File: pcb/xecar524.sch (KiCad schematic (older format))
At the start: 39 parts, among them J1 JTAG, J2 PROG, J3 Conn_02x02_Odd_Even, U1 MCP1703A-3302_SOT89, U2 Atari_XE_Cartridge_Connector, U3 XC95144XL-TQ100, U4 SST39VF040

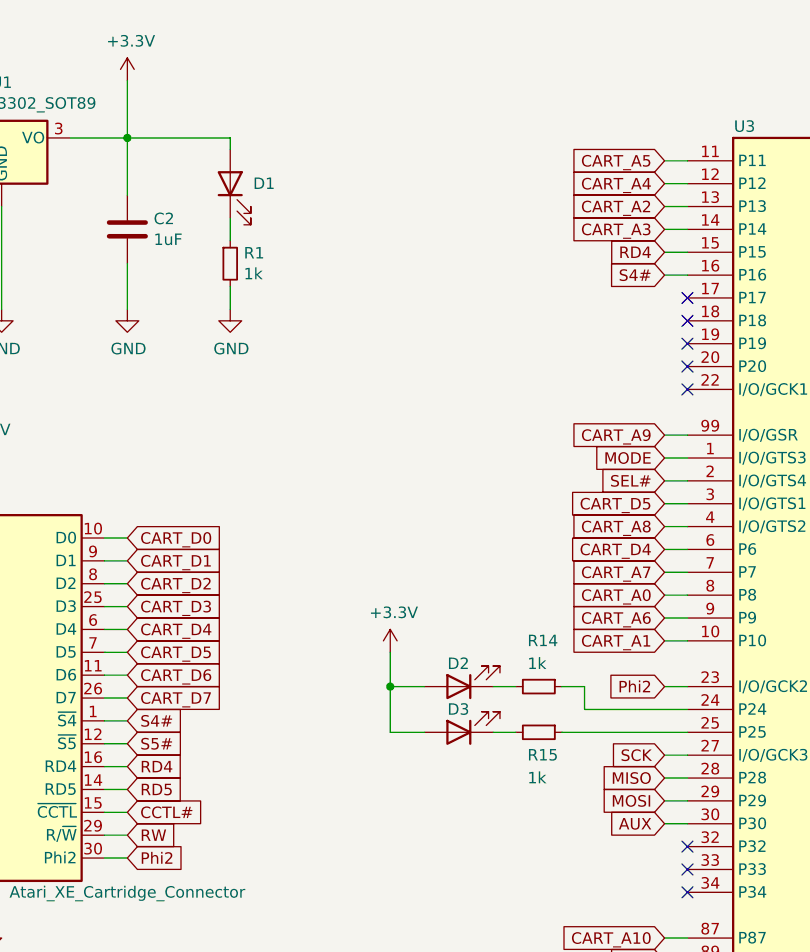
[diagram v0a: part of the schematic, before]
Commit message: PCB: Update LEDs and their current-setting resistors
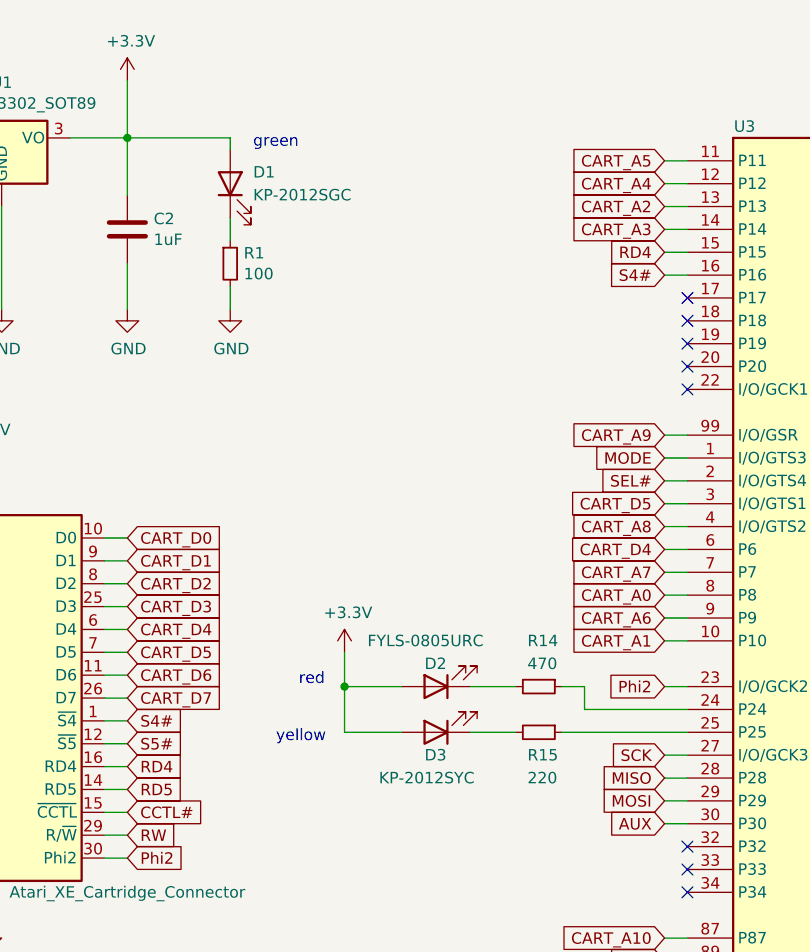
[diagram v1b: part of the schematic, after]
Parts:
- D1: value LED -> KP-2012SGC
- D2: value LED -> FYLS-0805URC
- D3: value LED -> KP-2012SYC
- R1: value 1k -> 100
- R14: value 1k -> 470
- R15: value 1k -> 220
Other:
- note added: "green"
- note added: "red"
- note added: "yellow"
- moved on the sheet: D2, D3
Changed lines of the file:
@@
 U 1 1 60C5727F
 P 2800 1350
-F 0 "D1" V 2800 1250 50  0000 R CNN
-F 1 "LED" V 2748 1232 50  0001 R CNN
+F 0 "D1" V 2850 1250 50  0000 R CNN
+F 1 "KP-2012SGC" V 2750 1250 50  0000 R CNN
 F 2 "Diode_SMD:D_0805_2012Metric_Pad1.15x1.40mm_HandSolder" H 2800 1350 50  0001 C CNN
 F 3 "~" H 2800 1350 50  0001 C CNN
@@
 P 2800 1700
 F 0 "R1" H 2859 1746 50  0000 L CNN
-F 1 "1k" H 2859 1655 50  0000 L CNN
+F 1 "100" H 2859 1655 50  0000 L CNN
 F 2 "Resistor_SMD:R_0805_2012Metric_Pad1.20x1.40mm_HandSolder" H 2800 1700 50  0001 C CNN
 F 3 "~" H 2800 1700 50  0001 C CNN
@@
 L Device:LED D3
 U 1 1 60DA2752
-P 3800 3750
-F 0 "D3" H 3850 3650 50  0000 R CNN
-F 1 "LED" H 4000 3700 50  0001 R CNN
-F 2 "Diode_SMD:D_0805_2012Metric_Pad1.15x1.40mm_HandSolder" H 3800 3750 50  0001 C CNN
-F 3 "~" H 3800 3750 50  0001 C CNN
-	1    3800 3750
+P 3700 3750
+F 0 "D3" H 3750 3850 50  0000 R CNN
+F 1 "KP-2012SYC" H 3950 3950 50  0000 R CNN
+F 2 "Diode_SMD:D_0805_2012Metric_Pad1.15x1.40mm_HandSolder" H 3700 3750 50  0001 C CNN
+F 3 "~" H 3700 3750 50  0001 C CNN
+	1    3700 3750
 	-1   0    0    1
 $EndComp
@@
 L Device:LED D2
 U 1 1 60DA08E3
-P 3800 3550
-F 0 "D2" H 3850 3450 50  0000 R CNN
-F 1 "LED" H 3748 3432 50  0001 R CNN
-F 2 "Diode_SMD:D_0805_2012Metric_Pad1.15x1.40mm_HandSolder" H 3800 3550 50  0001 C CNN
-F 3 "~" H 3800 3550 50  0001 C CNN
-	1    3800 3550
+P 3700 3550
+F 0 "D2" H 3750 3450 50  0000 R CNN
+F 1 "FYLS-0805URC" H 4000 3350 50  0000 R CNN
+F 2 "Diode_SMD:D_0805_2012Metric_Pad1.15x1.40mm_HandSolder" H 3700 3550 50  0001 C CNN
+F 3 "~" H 3700 3550 50  0001 C CNN
+	1    3700 3550
 	-1   0    0    1
 $EndComp
@@
 P 4150 3550
 F 0 "R14" V 3950 3500 50  0000 L CNN
-F 1 "1k" V 4050 3500 50  0000 L CNN
+F 1 "470" V 4050 3500 50  0000 L CNN
 F 2 "Resistor_SMD:R_0805_2012Metric_Pad1.20x1.40mm_HandSolder" H 4150 3550 50  0001 C CNN
 F 3 "~" H 4150 3550 50  0001 C CNN
@@
 P 4150 3750
 F 0 "R15" V 4250 3700 50  0000 L CNN
-F 1 "1k" V 4350 3700 50  0000 L CNN
+F 1 "220" V 4350 3700 50  0000 L CNN
 F 2 "Resistor_SMD:R_0805_2012Metric_Pad1.20x1.40mm_HandSolder" H 4150 3750 50  0001 C CNN
 F 3 "~" H 4150 3750 50  0001 C CNN
@@
 L power:+3.3V #PWR0117
 U 1 1 60DD9B32
-P 3500 3400
-F 0 "#PWR0117" H 3500 3250 50  0001 C CNN
-F 1 "+3.3V" H 3515 3573 50  0000 C CNN
-F 2 "" H 3500 3400 50  0001 C CNN
-F 3 "" H 3500 3400 50  0001 C CNN
-	1    3500 3400
-	1    0    0    -1
-$EndComp
-Wire Wire Line
-	3500 3400 3500 3550
-Wire Wire Line
-	3500 3550 3650 3550
+P 3300 3400
+F 0 "#PWR0117" H 3300 3250 50  0001 C CNN
+F 1 "+3.3V" H 3315 3573 50  0000 C CNN
+F 2 "" H 3300 3400 50  0001 C CNN
+F 3 "" H 3300 3400 50  0001 C CNN
+	1    3300 3400
+	1    0    0    -1
+$EndComp
+Wire Wire Line
+	3300 3400 3300 3550
 Wire Wire Line
 	4800 3750 4250 3750
 Wire Wire Line
-	3650 3750 3500 3750
-Wire Wire Line
-	3500 3750 3500 3550
-Connection ~ 3500 3550
+	3300 3750 3300 3550
+Connection ~ 3300 3550
 Wire Wire Line
 	4350 3550 4350 3650
@@
 	4350 3650 4800 3650
 Wire Wire Line
-	3950 3550 4050 3550
-Wire Wire Line
-	3950 3750 4050 3750
+	3850 3550 4050 3550
+Wire Wire Line
+	3850 3750 4050 3750
 Wire Wire Line
 	4250 3550 4350 3550
@@
 	-1   0    0    -1
 $EndComp
+Text Notes 2900 1200 0    50   ~ 0
+green
+Text Notes 3100 3550 0    50   ~ 0
+red
+Text Notes 3000 3800 0    50   ~ 0
+yellow
+Wire Wire Line
+	3300 3550 3550 3550
+Wire Wire Line
+	3300 3750 3550 3750
 $EndSCHEMATC

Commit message: PCB: Exchange cfg signals
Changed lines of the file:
@@
 	2400 5800 2400 5500
 Connection ~ 2400 5500
-Text GLabel 6900 1550 2    50   Input ~ 0
+Text GLabel 6900 1450 2    50   Input ~ 0
 CFG0
 Wire Wire Line
 	6900 1450 6800 1450
-Text GLabel 6900 1450 2    50   Input ~ 0
+Text GLabel 6900 1550 2    50   Input ~ 0
 CFG1
 Wire Wire Line
 	6900 1550 6800 1550
-$Comp
-L Connector_Generic:Conn_02x02_Odd_Even J3
-U 1 1 61481D01
-P 1600 5600
-F 0 "J3" H 1650 5725 50  0000 C CNN
-F 1 "Conn_02x02_Odd_Even" H 1650 5726 50  0001 C CNN
-F 2 "Connector_PinHeader_2.54mm:PinHeader_2x02_P2.54mm_Horizontal" H 1600 5600 50  0001 C CNN
-F 3 "~" H 1600 5600 50  0001 C CNN
-	1    1600 5600
-	-1   0    0    -1
-$EndComp
 Text Notes 2900 1200 0    50   ~ 0
 green
@@
 Wire Wire Line
 	3300 3750 3550 3750
+$Comp
+L Connector_Generic:Conn_02x02_Odd_Even J3
+U 1 1 61481D01
+P 1600 5700
+F 0 "J3" H 1650 5500 50  0000 C CNN
+F 1 "Conn_02x02_Odd_Even" H 1650 5826 50  0001 C CNN
+F 2 "Connector_PinHeader_2.54mm:PinHeader_2x02_P2.54mm_Horizontal" H 1600 5700 50  0001 C CNN
+F 3 "~" H 1600 5700 50  0001 C CNN
+	1    1600 5700
+	-1   0    0    1
+$EndComp
 $EndSCHEMATC

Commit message: PCB: Decrease yellow LED brightness
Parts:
- R15: value 220 -> 470
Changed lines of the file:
@@
 P 4150 3750
 F 0 "R15" V 4250 3700 50  0000 L CNN
-F 1 "220" V 4350 3700 50  0000 L CNN
+F 1 "470" V 4350 3700 50  0000 L CNN
 F 2 "Resistor_SMD:R_0805_2012Metric_Pad1.20x1.40mm_HandSolder" H 4150 3750 50  0001 C CNN
 F 3 "~" H 4150 3750 50  0001 C CNN

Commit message: PCB, PLD: Integrate R-Time 8 emulator
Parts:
- removed J2: PROG, Connector_PinHeader_2.54mm:PinHeader_1x08_P2.54mm_Horizontal_HighProfile, symbol Connector:Conn_01x08_Male
- removed R10, R11, R12, R13, R8, R9: 100, Resistor_SMD:R_0805_2012Metric_Pad1.20x1.40mm_HandSolder, symbol Device:R_Small
- removed R7: 10k, Resistor_SMD:R_0805_2012Metric_Pad1.20x1.40mm_HandSolder, symbol Device:R_Small
- U4: footprint Package_LCC:PLCC-32_THT-Socket -> Miscellaneous:PLCC-32_SMD-Socket
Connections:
- net labels added: PMCS1, PMD0, PMD1, PMD2, PMD3, PMRD, PMWR
- net labels removed: AUX, MISO, MODE, MOSI, SCK, SEL#
- wire segments 273 -> 254
- no-connect marks 12 -> 11
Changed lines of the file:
@@
 $Descr A4 11693 8268
 encoding utf-8
-Sheet 1 1
+Sheet 1 2
 Title ""
 Date ""
@@
 F 3 "http://atariki.krap.pl/index.php/Gniazdo_cartridge%27a" H 1700 3800 50  0001 C CNN
 	1    1750 3600
-	1    0    0    -1
-$EndComp
-$Comp
-L CPLD_Xilinx:XC95144XL-TQ100 U3
-U 1 1 61014D55
-P 5800 3650
-F 0 "U3" H 5050 6200 50  0000 C CNN
-F 1 "XC95144XL-TQ100" H 6600 1100 50  0000 C CNN
-F 2 "Package_QFP:TQFP-100_14x14mm_P0.5mm" H 5800 3650 50  0001 C CNN
-F 3 "https://www.xilinx.com/support/documentation/data_sheets/ds056.pdf" H 5800 3650 50  0001 C CNN
-	1    5800 3650
 	1    0    0    -1
 $EndComp
@@
 Wire Wire Line
 	6900 5450 6800 5450
-Text GLabel 6900 5550 2    50   Input ~ 0
+Text GLabel 6900 2450 2    50   Input ~ 0
 WE#
 Wire Wire Line
 	6900 5550 6800 5550
-Text GLabel 6900 2450 2    50   Input ~ 0
+Text GLabel 6900 2550 2    50   Input ~ 0
 ROM_A17
 Wire Wire Line
 	6900 2450 6800 2450
-Text GLabel 6900 2550 2    50   Input ~ 0
+Text GLabel 6900 2650 2    50   Input ~ 0
 ROM_A14
 Wire Wire Line
@@
 Wire Wire Line
 	6900 2650 6800 2650
-Text GLabel 6900 2650 2    50   Input ~ 0
+Text GLabel 6900 2750 2    50   Input ~ 0
 ROM_A13
+Text GLabel 6900 3650 2    50   Input ~ 0
+ROM_D6
 Text GLabel 6900 3550 2    50   Input ~ 0
-ROM_D6
+ROM_D7
+Text GLabel 6900 2150 2    50   Input ~ 0
+CE#
+Text GLabel 6900 1750 2    50   Input ~ 0
+OE#
+Wire Wire Line
+	6800 3550 6900 3550
+Wire Wire Line
+	6800 2050 6900 2050
+Wire Wire Line
+	6800 3650 6900 3650
+Wire Wire Line
+	6800 2150 6900 2150
 Text GLabel 6900 2050 2    50   Input ~ 0
-ROM_D7
-Text GLabel 6900 3650 2    50   Input ~ 0
-CE#
-Text GLabel 6900 2150 2    50   Input ~ 0
-OE#
-Wire Wire Line
-	6800 3550 6900 3550
-Wire Wire Line
-	6800 2050 6900 2050
-Wire Wire Line
-	6800 3650 6900 3650
-Wire Wire Line
-	6800 2150 6900 2150
-Text GLabel 6900 1750 2    50   Input ~ 0
 ROM_A10
 Wire Wire Line
@@
 Wire Wire Line
 	9450 5850 9200 5850
-$Comp
-L Connector:Conn_01x08_Male J2
-U 1 1 61185382
-P 1100 7050
-F 0 "J2" H 1208 7531 50  0000 C CNN
-F 1 "PROG" H 1208 7440 50  0000 C CNN
-F 2 "Connector_PinHeader_2.54mm:PinHeader_1x08_P2.54mm_Horizontal_HighProfile" H 1100 7050 50  0001 C CNN
-F 3 "~" H 1100 7050 50  0001 C CNN
-	1    1100 7050
-	1    0    0    -1
-$EndComp
-$Comp
-L Device:R_Small R10
-U 1 1 6118A684
-P 2000 7150
-F 0 "R10" V 1950 7000 50  0000 C CNN
-F 1 "100" V 1950 7300 50  0000 C CNN
-F 2 "Resistor_SMD:R_0805_2012Metric_Pad1.20x1.40mm_HandSolder" H 2000 7150 50  0001 C CNN
-F 3 "~" H 2000 7150 50  0001 C CNN
-	1    2000 7150
-	0    1    1    0
-$EndComp
-$Comp
-L Device:R_Small R11
-U 1 1 6118A8DE
-P 2000 7250
-F 0 "R11" V 1950 7100 50  0000 C CNN
-F 1 "100" V 1950 7400 50  0000 C CNN
-F 2 "Resistor_SMD:R_0805_2012Metric_Pad1.20x1.40mm_HandSolder" H 2000 7250 50  0001 C CNN
-F 3 "~" H 2000 7250 50  0001 C CNN
-	1    2000 7250
-	0    1    1    0
-$EndComp
-$Comp
-L Device:R_Small R12
-U 1 1 6118A8E8
-P 2000 7350
-F 0 "R12" V 1950 7200 50  0000 C CNN
-F 1 "100" V 1950 7500 50  0000 C CNN
-F 2 "Resistor_SMD:R_0805_2012Metric_Pad1.20x1.40mm_HandSolder" H 2000 7350 50  0001 C CNN
-F 3 "~" H 2000 7350 50  0001 C CNN
-	1    2000 7350
-	0    1    1    0
-$EndComp
-$Comp
-L Device:R_Small R13
-U 1 1 6118A8F2
-P 2000 7450
-F 0 "R13" V 1950 7300 50  0000 C CNN
-F 1 "100" V 1950 7600 50  0000 C CNN
-F 2 "Resistor_SMD:R_0805_2012Metric_Pad1.20x1.40mm_HandSolder" H 2000 7450 50  0001 C CNN
-F 3 "~" H 2000 7450 50  0001 C CNN
-	1    2000 7450
-	0    1    1    0
-$EndComp
-$Comp
-L Device:R_Small R9
-U 1 1 6118A8FC
-P 2000 7050
-F 0 "R9" V 1950 6900 50  0000 C CNN
-F 1 "100" V 1950 7200 50  0000 C CNN
-F 2 "Resistor_SMD:R_0805_2012Metric_Pad1.20x1.40mm_HandSolder" H 2000 7050 50  0001 C CNN
-F 3 "~" H 2000 7050 50  0001 C CNN
-	1    2000 7050
-	0    1    1    0
-$EndComp
-Wire Wire Line
-	1300 7250 1900 7250
-Wire Wire Line
-	1300 7350 1900 7350
-Wire Wire Line
-	1300 7450 1900 7450
-Wire Wire Line
-	2100 7450 2500 7450
-Wire Wire Line
-	2500 7350 2100 7350
-Wire Wire Line
-	2100 7250 2500 7250
-Wire Wire Line
-	2500 7150 2100 7150
-$Comp
-L power:GND #PWR01
-U 1 1 611A4CBD
-P 1400 6850
-F 0 "#PWR01" H 1400 6600 50  0001 C CNN
-F 1 "GND" V 1405 6722 50  0000 R CNN
-F 2 "" H 1400 6850 50  0001 C CNN
-F 3 "" H 1400 6850 50  0001 C CNN
-	1    1400 6850
-	0    -1   -1   0
-$EndComp
-Wire Wire Line
-	1400 6850 1300 6850
-$Comp
-L Device:R_Small R8
-U 1 1 611CD721
-P 2000 6950
-F 0 "R8" V 1950 6800 50  0000 C CNN
-F 1 "100" V 1950 7100 50  0000 C CNN
-F 2 "Resistor_SMD:R_0805_2012Metric_Pad1.20x1.40mm_HandSolder" H 2000 6950 50  0001 C CNN
-F 3 "~" H 2000 6950 50  0001 C CNN
-	1    2000 6950
-	0    1    1    0
-$EndComp
-$Comp
-L Device:R_Small R7
-U 1 1 611CDA81
-P 2000 6850
-F 0 "R7" V 1950 6700 50  0000 C CNN
-F 1 "10k" V 1950 7000 50  0000 C CNN
-F 2 "Resistor_SMD:R_0805_2012Metric_Pad1.20x1.40mm_HandSolder" H 2000 6850 50  0001 C CNN
-F 3 "~" H 2000 6850 50  0001 C CNN
-	1    2000 6850
-	0    1    1    0
-$EndComp
-Wire Wire Line
-	1300 7150 1900 7150
-Wire Wire Line
-	1300 7050 1900 7050
-Wire Wire Line
-	2500 6950 2300 6950
-Wire Wire Line
-	2100 7050 2500 7050
-Text GLabel 2500 6950 2    50   Input ~ 0
-MODE
-Text GLabel 2500 7050 2    50   Input ~ 0
-SEL#
-Text GLabel 2500 7250 2    50   Input ~ 0
-MOSI
-Text GLabel 2500 7350 2    50   Input ~ 0
-MISO
-$Comp
-L power:+3.3V #PWR02
-U 1 1 611B9BAC
-P 1750 6550
-F 0 "#PWR02" H 1750 6400 50  0001 C CNN
-F 1 "+3.3V" H 1765 6678 50  0000 L CNN
-F 2 "" H 1750 6550 50  0001 C CNN
-F 3 "" H 1750 6550 50  0001 C CNN
-	1    1750 6550
-	1    0    0    -1
-$EndComp
-Wire Wire Line
-	1300 6950 1900 6950
-Wire Wire Line
-	1300 6750 1750 6750
-Wire Wire Line
-	1750 6750 1750 6550
-Wire Wire Line
-	1900 6850 1750 6850
-Wire Wire Line
-	1750 6850 1750 6750
-Connection ~ 1750 6750
-Wire Wire Line
-	2100 6850 2300 6850
-Wire Wire Line
-	2300 6850 2300 6950
-Connection ~ 2300 6950
-Wire Wire Line
-	2300 6950 2100 6950
 Wire Wire Line
 	8150 5850 8750 5850
@@
 Wire Wire Line
 	6800 2750 6900 2750
-Text GLabel 6900 2750 2    50   Input ~ 0
+Text GLabel 6900 2850 2    50   Input ~ 0
 ROM_A8
 Wire Wire Line
 	6800 2850 6900 2850
-Text GLabel 6900 2850 2    50   Input ~ 0
+Text GLabel 6900 2950 2    50   Input ~ 0
 ROM_A9
 Wire Wire Line
 	6900 2950 6800 2950
-Text GLabel 6900 2950 2    50   Input ~ 0
+Text GLabel 6900 1650 2    50   Input ~ 0
 ROM_A11
 Wire Wire Line
@@
 Wire Wire Line
 	6900 3750 6800 3750
+Text GLabel 6900 3750 2    50   Input ~ 0
+ROM_D5
 Text GLabel 6900 3850 2    50   Input ~ 0
-ROM_D5
-Text GLabel 6900 3750 2    50   Input ~ 0
 ROM_D4
 Text GLabel 6900 3950 2    50   Input ~ 0
 ROM_D3
-Text GLabel 6900 4050 2    50   Input ~ 0
+Text GLabel 6900 4150 2    50   Input ~ 0
 ROM_D1
 Wire Wire Line
@@
 Wire Wire Line
 	6900 4150 6800 4150
-Text GLabel 6900 4150 2    50   Input ~ 0
+Text GLabel 6900 4050 2    50   Input ~ 0
 ROM_D2
-Text GLabel 4700 2550 0    50   Input ~ 0
-MODE
-Text GLabel 4700 2650 0    50   Input ~ 0
-SEL#
+Text GLabel 4700 3950 0    50   Input ~ 0
+PMCS1
 Text GLabel 4700 4050 0    50   Input ~ 0
-MOSI
-Text GLabel 4700 3950 0    50   Input ~ 0
-MISO
-Wire Wire Line
-	4800 2650 4700 2650
+PMRD
+Text GLabel 6900 1250 2    50   Input ~ 0
+PMD2
+Text GLabel 4700 4450 0    50   Input ~ 0
+PMD1
 Wire Wire Line
 	4700 4150 4800 4150
@@
 Wire Wire Line
 	4800 3850 4700 3850
-Wire Wire Line
-	4700 2550 4800 2550
 $Comp
 L Device:C_Polarized C11
@@
 F 0 "U4" H 9300 4500 50  0000 C CNN
 F 1 "SST39VF040" H 9950 2400 50  0000 C CNN
-F 2 "Package_LCC:PLCC-32_THT-Socket" H 9700 3450 50  0001 C CNN
+F 2 "Miscellaneous:PLCC-32_SMD-Socket" H 9700 3450 50  0001 C CNN
 F 3 "https://ww1.microchip.com/downloads/en/DeviceDoc/20005023B.pdf" H 9650 3750 50  0001 C CNN
 	1    9650 3450
@@
 Wire Wire Line
 	9050 4350 8950 4350
-Text GLabel 6900 1650 2    50   Input ~ 0
+Text GLabel 6900 5550 2    50   Input ~ 0
 ROM_A18
 Wire Wire Line
 	6900 1650 6800 1650
+Text GLabel 6900 1350 2    50   Input ~ 0
+PMD3
 Text GLabel 4700 4150 0    50   Input ~ 0
-AUX
-Text GLabel 4700 3850 0    50   Input ~ 0
-SCK
+PMD0
 Wire Wire Line
 	6900 3150 6800 3150
 Text GLabel 6900 3150 2    50   Input ~ 0
 Phi2
-Text GLabel 2500 7450 2    50   Input ~ 0
-SCK
-Text GLabel 2500 7150 2    50   Input ~ 0
-AUX
 $Comp
 L Device:LED D3
@@
 NoConn ~ 4800 4250
 NoConn ~ 4800 4350
-NoConn ~ 4800 4450
+NoConn ~ 4800 2650
 NoConn ~ 6800 1950
 NoConn ~ 6800 1850
-NoConn ~ 6800 1350
-NoConn ~ 6800 1250
+NoConn ~ 4800 2550
 NoConn ~ 4800 1850
 NoConn ~ 4800 1950
@@
 	-1   0    0    1
 $EndComp
+$Sheet
+S 2350 6650 1200 650
+U 60FB7BC7
+F0 "rtime8" 50
+F1 "rtime8.sch" 50
+$EndSheet
+$Comp
+L CPLD_Xilinx:XC95144XL-TQ100 U3
+U 1 1 61014D55
+P 5800 3650
+F 0 "U3" H 5050 6200 50  0000 C CNN
+F 1 "XC95144XL-TQ100" H 6600 1100 50  0000 C CNN
+F 2 "Package_QFP:TQFP-100_14x14mm_P0.5mm" H 5800 3650 50  0001 C CNN
+F 3 "https://www.xilinx.com/support/documentation/data_sheets/ds056.pdf" H 5800 3650 50  0001 C CNN
+	1    5800 3650
+	1    0    0    -1
+$EndComp
+Text GLabel 4700 3850 0    50   Input ~ 0
+PMWR
+Wire Wire Line
+	6900 1350 6800 1350
+Wire Wire Line
+	6800 1250 6900 1250
+Wire Wire Line
+	4700 4450 4800 4450
 $EndSCHEMATC

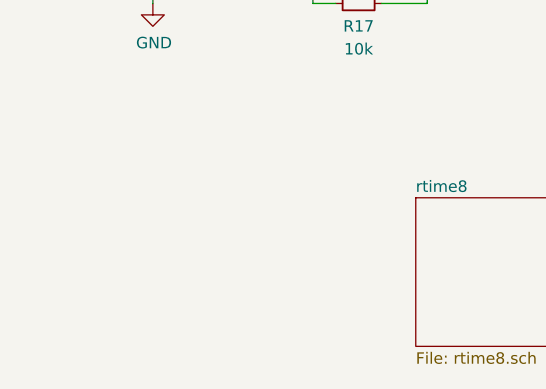
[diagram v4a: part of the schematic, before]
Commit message: PCB: Add OSHW symbol on schematic
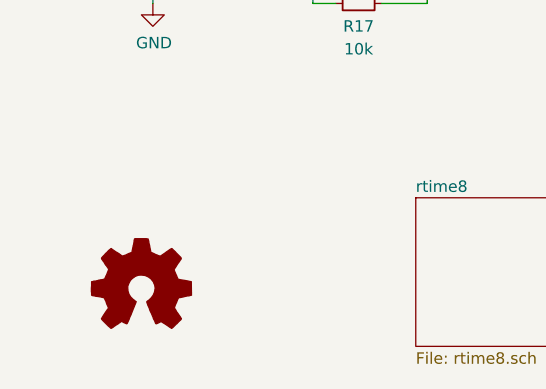
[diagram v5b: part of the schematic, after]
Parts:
- added LOGO1: Logo_Open_Hardware_Small, Symbol:OSHW-Symbol_13.4x12mm_Copper, symbol Graphic:Logo_Open_Hardware_Small
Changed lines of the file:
@@
 Wire Wire Line
 	4700 4450 4800 4450
+$Comp
+L Graphic:Logo_Open_Hardware_Small LOGO1
+U 1 1 6123A3D4
+P 1150 7050
+F 0 "LOGO1" H 1150 7325 50  0001 C CNN
+F 1 "Logo_Open_Hardware_Small" H 1150 6825 50  0001 C CNN
+F 2 "Symbol:OSHW-Symbol_13.4x12mm_Copper" H 1150 7050 50  0001 C CNN
+F 3 "~" H 1150 7050 50  0001 C CNN
+	1    1150 7050
+	1    0    0    -1
+$EndComp
 $EndSCHEMATC
